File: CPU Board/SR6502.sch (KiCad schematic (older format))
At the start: 31 parts, among them J1 Conn_01x40_Female, SW1 RESET, SW2 SWA, SW3 SWA, SW4 SWA, SW5 SWA, SW6 SWA, U2 WD65C02_, U3 74HC00, U4 28C256, U5 CY62256-70PC, U6 WD65C22, U7 WC1602A, X1 1mhz

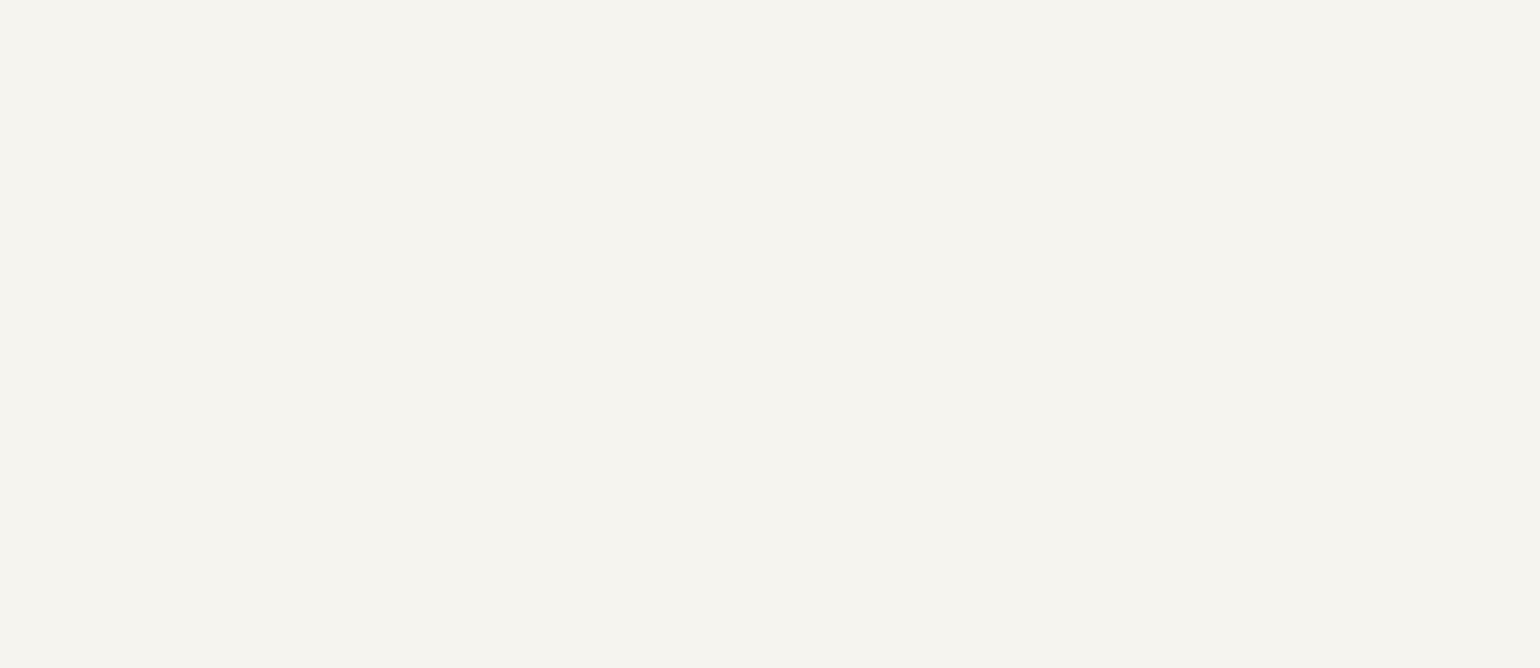
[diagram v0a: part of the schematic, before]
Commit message: Updated memory map, starting working on serial console
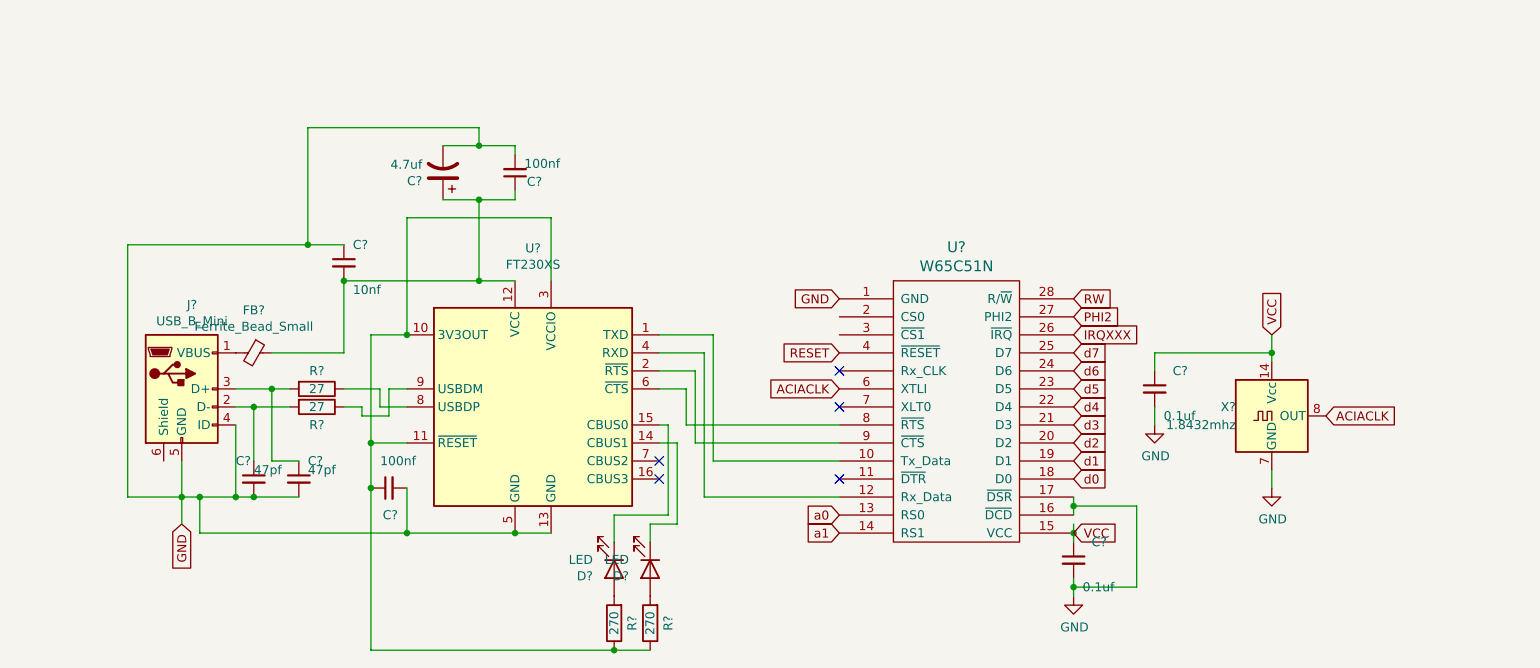
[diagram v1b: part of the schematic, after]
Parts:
- added C? (x2): 0.1uf, Capacitor_THT:C_Disc_D5.0mm_W2.5mm_P2.50mm, symbol Device:C_Small
- added C? (x2): 47pf, Capacitor_THT:C_Disc_D5.0mm_W2.5mm_P2.50mm, symbol Device:C_Small
- added C?: 10nf, Capacitor_THT:C_Disc_D5.0mm_W2.5mm_P2.50mm, symbol Device:C_Small
- added C? (x2): 100nf, Capacitor_THT:C_Disc_D5.0mm_W2.5mm_P2.50mm, symbol Device:C_Small
- added C?: 4.7uf, symbol Device:CP1
- added D? (x2): LED, symbol Device:LED
- added FB?: Ferrite_Bead_Small, symbol Device:Ferrite_Bead_Small
- added J?: USB_B_Mini, symbol Connector:USB_B_Mini
- added R? (x2): 270, Resistor_THT:R_Axial_DIN0204_L3.6mm_D1.6mm_P1.90mm_Vertical, symbol Device:R
- added R? (x2): 27, Resistor_THT:R_Axial_DIN0204_L3.6mm_D1.6mm_P1.90mm_Vertical, symbol Device:R
- added U?: W65C51N, symbol 65xx:W65C51N
- added U?: FT230XS, Package_SO:SSOP-16_3.9x4.9mm_P0.635mm, symbol Interface_USB:FT230XS
- added X?: 1.8432mhz, Package_DIP:DIP-14_W7.62mm_Socket, symbol Oscillator:ACO-xxxMHz
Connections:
- net GND: now also C?.1, C?.2, C?.2, C?.2, C?.2, C?.2, C?.2, C?.2, J?.4 (ID), J?.5 (GND), U?.1 (GND), U?.13 (GND), U?.16 (~DCD), U?.17 (~DSR), U?.5 (GND), X?.7 (GND)
- net PHI2: now also U?.27 (PHI2)
- net RESET: now also U?.4 (~RESET)
- net RW: now also U?.28 (R/~W)
- net VCC: now also C?.1, C?.1, U?.15 (VCC), X?.14 (Vcc)
- net a0: now also U?.13 (RS0)
- net a1: now also U?.14 (RS1)
- net d0: now also U?.18 (D0)
- net d1: now also U?.19 (D1)
- net d2: now also U?.20 (D2)
- net d3: now also U?.21 (D3)
- net d4: now also U?.22 (D4)
- net d5: now also U?.23 (D5)
- net d6: now also U?.24 (D6)
- net d7: now also U?.25 (D7)
- new net: U?.1 (TXD), U?.10 (Tx_Data)
- new net: U?.12 (Rx_Data), U?.4 (RXD)
- new net: U?.6 (~CTS), U?.8 (~RTS)
- new net: U?.2 (~RTS), U?.9 (~CTS)
- new net: C?.1, R?.1, R?.1, U?.10 (3V3OUT), U?.11 (~RESET), U?.3 (VCCIO)
- new net: C?.1, C?.1, C?.2, FB?.1, U?.12 (VCC)
- new net: D?.1 (K), U?.14 (CBUS1)
- new net: D?.1 (K), U?.15 (CBUS0)
- new net: R?.1, U?.8 (USBDP)
- new net: R?.1, U?.9 (USBDM)
- new net: D?.2 (A), R?.2 (x2)
- new net: FB?.2, J?.1 (VBUS)
- new net: C?.1, J?.2 (D-), R?.2
- new net: C?.1, J?.3 (D+), R?.2
- new net ACIACLK: U?.6 (XTLI), X?.8 (OUT)
- new net IRQXXX: U?.26 (~IRQ)
- no-connect marks 20 -> 25

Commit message: fixed errors in schematic (5 missing traces on pcb), did not export gerber yet
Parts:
- removed R3, R4, R5, R6, R7: 1k, Resistor_THT:R_Axial_DIN0204_L3.6mm_D1.6mm_P1.90mm_Vertical, symbol Device:R
- removed SW2, SW3, SW4, SW5, SW6: SWA, Button_Switch_THT:SW_Tactile_Straight_KSA0Axx1LFTR, symbol Switch:SW_Push
- added R? (x2): 3.3k, Resistor_THT:R_Axial_DIN0204_L3.6mm_D1.6mm_P1.90mm_Vertical, symbol Device:R
- J1: value Conn_01x40_Female -> Conn_02x40_Female; footprint Connector_PinSocket_2.54mm:PinSocket_1x40_P2.54mm_Vertical -> Connector_PinSocket_2.54mm:PinSocket_2x40_P2.54mm_Vertical; symbol Connector:Conn_01x40_Female -> Connector_Generic:Conn_02x40_Top_Bottom
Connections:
- net VCC: now also R?.1, R?.1; no longer U2.2 (RDY), U2.36 (BE), U3.1, U3.2
- net VIA1_CS2: now also U6.23 (~CS2)
- net a0: now also U6.38 (RS0)
- net a1: now also U6.37 (RS1)
- net a2: now also U6.36 (RS2)
- net a3: now also U6.35 (RS3)
- net DISPE: now reaches U6.9 (PA7), U7.6 (E)
- net VP: now reaches U2.1 (~VP)
- net VP: now also J1.34 (Pin_34)
- net PHI1O: now reaches U2.3 (PHI1out)
- net PHI1O: now also J1.36 (Pin_36)
- net SO: now reaches U2.38 (~SO)
- net SO: now also J1.35 (Pin_35)
- net PHI2O: now reaches U2.39 (PHI2out)
- net PHI2O: now also J1.37 (Pin_37)
- net ML: now reaches U2.5 (~ML)
- net ML: now also J1.33 (Pin_33)
- net SYNC: now reaches U2.7 (SYNC)
- net SYNC: now also J1.32 (Pin_32)
- net READY: now reaches J1.30 (Pin_30)
- net READY: now also U2.2 (RDY), R?.2
- net BE: now reaches J1.31 (Pin_31)
- net BE: now also U2.36 (BE), R?.2
- net ACIACLK: no longer names the net of U?.6 (XTLI), X?.8 (OUT)
- net B1: no longer names the net of U6.2 (PA0)
- net B2: no longer names the net of U6.3 (PA1)
- net B3: no longer names the net of U6.4 (PA2)
- net B4: no longer names the net of U6.5 (PA3)
- net B5: no longer names the net of U6.6 (PA4)
- no-connect marks 25 -> 22
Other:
- moved on the sheet: C?, U3A, X?

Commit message: changed memory map, added ACIA and 2nd VIA, irq matrix, added backplane pcb
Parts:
- removed C? (x2): 47pf, Capacitor_THT:C_Disc_D5.0mm_W2.5mm_P2.50mm, symbol Device:C_Small
- removed C?: 10nf, Capacitor_THT:C_Disc_D5.0mm_W2.5mm_P2.50mm, symbol Device:C_Small
- removed C? (x2): 100nf, Capacitor_THT:C_Disc_D5.0mm_W2.5mm_P2.50mm, symbol Device:C_Small
- removed C?: 4.7uf, symbol Device:CP1
- removed D? (x2): LED, symbol Device:LED
- removed FB?: Ferrite_Bead_Small, symbol Device:Ferrite_Bead_Small
- removed J?: USB_B_Mini, symbol Connector:USB_B_Mini
- removed R2: 1k, Resistor_THT:R_Axial_DIN0204_L3.6mm_D1.6mm_P1.90mm_Vertical, symbol Device:R
- removed R? (x2): 270, Resistor_THT:R_Axial_DIN0204_L3.6mm_D1.6mm_P1.90mm_Vertical, symbol Device:R
- removed R? (x2): 3.3k, Resistor_THT:R_Axial_DIN0204_L3.6mm_D1.6mm_P1.90mm_Vertical, symbol Device:R
- removed R? (x2): 27, Resistor_THT:R_Axial_DIN0204_L3.6mm_D1.6mm_P1.90mm_Vertical, symbol Device:R
- removed unit 4 of U3
- removed unit 3 of U3
- removed U?: FT230XS, Package_SO:SSOP-16_3.9x4.9mm_P0.635mm, symbol Interface_USB:FT230XS
- added C? (x5): 0.1uf, Capacitor_THT:C_Disc_D5.0mm_W2.5mm_P2.50mm, symbol Device:C
- added D? (x17): LED, symbol Device:LED
- added J?: Conn_02x12_Odd_Even_MountingPin, symbol Connector_Generic_MountingPin:Conn_02x12_Odd_Even_MountingPin
- added J? (x2): Conn_01x10_Female, symbol Connector:Conn_01x10_Female
- added J?: 5VDC INPUT, symbol Connector:Barrel_Jack
- added J?: ACIA1, symbol Connector:Conn_01x11_Female
- added R? (x17): 220, symbol Device:R_Small
- added RN?: 1k, Resistor_THT:R_Array_SIP6, symbol Device:R_Network05
- added RN? (x2): 3.3k, Resistor_THT:R_Array_SIP10, symbol Device:R_Network09
- added SW? (x5): SW_Push, symbol Switch:SW_Push
- added SW? (x2): SW_DIP_x08, symbol Switch:SW_DIP_x08
- added U? (x7): 74HC00, Package_DIP:DIP-14_W7.62mm_Socket, symbol 74xx:74HC00
- added U? (x2): 74LS30, symbol 74xx:74LS30
- added U? (x2): 74LS138, symbol 74xx:74LS138
- added U? (x3): 74HC21, symbol 74xx:74LS21
- R1: value 1k -> 3.3k
- RV1: footprint Potentiometer_THT:Potentiometer_Vishay_43_Horizontal -> Potentiometer_THT:Potentiometer_Vishay_T73XW_Horizontal
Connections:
- net IRQXXX is gone; now on net IRQ4: U?.26 (~IRQ)
- net BE: now also SW?.16
- net GND: now also J1.80 (Pin_80), C?.2, C?.2, C?.2, C?.2, C?.2, J?.2, J?.6 (Pin_6), R?.2, R?.2, R?.2, R?.2, R?.2, R?.2, R?.2, R?.2, R?.2, R?.2, SW?.1, SW?.1, SW?.1, SW?.1, SW?.1, U?.4 (E1), U?.7 (GND), U?.7 (GND), U?.7 (GND), U?.8 (GND), U?.8 (GND); no longer U4.22 (~OE), U?.16 (~DCD), U?.17 (~DSR)
- net IRQ: now also D?.1 (K), U?.8; no longer U6.21 (~IRQ)
- net NMI: now also SW?.9
- net PHI1O: no longer J1.36 (Pin_36)
- net PHI2: now also U?.5
- net PHI2O: no longer J1.37 (Pin_37)
- net READY: now also SW?.15
- net ROM_CS: now also D?.1 (K), J?.1 (Pin_1); no longer U3.5
- net RW: now also J?.18 (Pin_18), J?.24 (Pin_24), U?.1, U?.2; no longer U5.27 (~WE), U6.22 (R/~W), U?.28 (R/~W)
- net SRAM_CS: now also D?.1 (K), J?.7 (Pin_7)
- net VCC: now also J1.79 (Pin_79), C?.1, C?.1, C?.1, C?.1, C?.1, J?.1, J?.1 (Pin_1), J?.16 (Pin_16), J?.2 (Pin_2), J?.20 (Pin_20), J?.6 (Pin_6), R?.2, R?.2, R?.2, R?.2, R?.2, R?.2, R?.2, RN?.1 (common), RN?.1 (common), RN?.1 (common), U?.14 (VCC), U?.14 (VCC), U?.14 (VCC), U?.16 (VCC), U?.16 (VCC), U?.6 (E3); no longer U4.27 (~WE)
- net VIA1_CS2: now also D?.1 (K), J?.13 (Pin_13); no longer U3.6
- net a10: now also U?.4
- net a11: now also U?.5
- net a12: now also U?.6
- net a13: now also U?.11; no longer U6.24 (CS1)
- net a14: now also U?.12; no longer U3.4, U5.22 (~OE)
- net a15: now also U?.10, U?.9
- net a4: now also U?.1 (A0)
- net a5: now also U?.2 (A1)
- net a6: now also U?.3 (A2)
- net a7: now also U?.4 (E1), U?.6 (E3)
- net a8: now also U?.2
- net a9: now also U?.3
- net VIA1PB0: now reaches U6.10 (PB0), U7.7 (D0)
- net VIA1PB0: now also J?.1 (Pin_1)
- net VIA1PB1: now reaches U6.11 (PB1), U7.8 (D1)
- net VIA1PB1: now also J?.2 (Pin_2)
- net VIA1PB2: now reaches U6.12 (PB2), U7.9 (D2)
- net VIA1PB2: now also J?.3 (Pin_3)
- net VIA1PB3: now reaches U6.13 (PB3), U7.10 (D3)
- net VIA1PB3: now also J?.4 (Pin_4)
- net VIA1PB4: now reaches U6.14 (PB4), U7.11 (D4)
- net VIA1PB4: now also J?.5 (Pin_5)
- net VIA1PB5: now reaches U6.15 (PB5), U7.12 (D5)
- net VIA1PB5: now also J?.6 (Pin_6)
- net VIA1PB6: now reaches U6.16 (PB6), U7.13 (D6)
- net VIA1PB6: now also J?.7 (Pin_7)
- net VIA1PB7: now reaches U6.17 (PB7), U7.14 (D7)
- net VIA1PB7: now also J?.8 (Pin_8)
- net VIA1CB1: now reaches U6.18 (CB1)
- net VIA1CB1: now also J?.9 (Pin_9)
- net VIA1CB2: now reaches U6.19 (CB2)
- net VIA1CB2: now also J?.10 (Pin_10)
- net VIA1PA0: now reaches U6.2 (PA0)
- net VIA1PA0: now also J?.1 (Pin_1), RN?.2 (R1), SW?.2
- net VIA1PA1: now reaches U6.3 (PA1)
- net VIA1PA1: now also J?.2 (Pin_2), RN?.3 (R2), SW?.2
- net VIA1CA2: now reaches U6.39 (CA2)
- net VIA1CA2: now also J?.10 (Pin_10)
- net VIA1PA2: now reaches U6.4 (PA2)
- net VIA1PA2: now also J?.3 (Pin_3), RN?.4 (R3), SW?.2
- net VIA1CA1: now reaches U6.40 (CA1)
- net VIA1CA1: now also J?.9 (Pin_9)
- net VIA1PA3: now reaches U6.5 (PA3)
- net VIA1PA3: now also J?.4 (Pin_4), RN?.5 (R4), SW?.2
- net VIA1PA4: now reaches U6.6 (PA4)
- net VIA1PA4: now also J?.5 (Pin_5), RN?.6 (R5), SW?.2
- net VIA1PA5: now reaches U6.7 (PA5), U7.4 (RS)
- net VIA1PA5: now also J?.6 (Pin_6)
- net VIA1PA6: now reaches U6.8 (PA6), U7.5 (R/W)
- net VIA1PA6: now also J?.7 (Pin_7)
- net IRQ1: now reaches J1.41 (Pin_41)
- net IRQ1: now also D?.1 (K), SW?.16, U?.1
- net IRQ2: now reaches J1.42 (Pin_42)
- net IRQ2: now also D?.1 (K), SW?.15, U?.2
- net IRQ3: now reaches J1.43 (Pin_43)
- net IRQ3: now also D?.1 (K), SW?.14, U?.4
- net IRQ4: now reaches J1.44 (Pin_44)
- net IRQ4: now also D?.1 (K), SW?.13, U?.5
- net IRQ5: now reaches J1.45 (Pin_45)
- net IRQ5: now also D?.1 (K), SW?.12, U?.9
- net IRQ6: now reaches J1.46 (Pin_46)
- net IRQ6: now also D?.1 (K), SW?.11, U?.10
- net IRQ7: now reaches J1.47 (Pin_47)
- net IRQ7: now also U6.21 (~IRQ), D?.1 (K), SW?.10, U?.12
- net $60XX: now reaches J1.48 (Pin_48)
- net $61XX: now reaches J1.49 (Pin_49)
- net $62XX: now reaches J1.50 (Pin_50)
- net $63XX: now reaches J1.51 (Pin_51)
- net $64XX: now reaches J1.52 (Pin_52)
- net $65XX: now reaches J1.53 (Pin_53)
- net $66XX: now reaches J1.54 (Pin_54)
- net $67XX: now reaches J1.55 (Pin_55)
- net ACIA_CLOCK: now reaches J1.78 (Pin_78)
- net ACIA_CLOCK: now also U?.6 (XTLI), X?.8 (OUT)
- net ACIA1_TXD: now reaches U?.10 (Tx_Data)
- net ACIA1_TXD: now also J?.5 (Pin_5)
- net ACIA1_DTR: now reaches U?.11 (~DTR)
- net ACIA1_DTR: now also J?.9 (Pin_9)
- net ACIA1_RXD: now reaches U?.12 (Rx_Data)
- net ACIA1_RXD: now also J?.4 (Pin_4)
- net ACIA1_CS0: now reaches U?.2 (CS0)
- net ACIA1_CS0: now also D?.2 (A), J?.19 (Pin_19)
- net ACIA2_CS1: now reaches U?.3 (~CS1)
- net ACIA2_CS1: now also D?.1 (K), J?.21 (Pin_21)
- net ACIA1_RTS: now reaches U?.8 (~RTS)
- net ACIA1_RTS: now also J?.11 (Pin_11)
- net ACIA1_CTS: now reaches U?.9 (~CTS)
- net ACIA1_CTS: now also J?.10 (Pin_10)
- net DISPE renamed VIA1PA7
- net VIA1PA7: now also J?.8 (Pin_8)
- new net: D?.2 (A), R?.1 (x15)
- new net: D?.1 (K), R?.1 (x2)
- new net: U?.13, U?.6
- new net: RN?.2 (R1), SW?.1 (x2)
- new net: RN?.3 (R2), SW?.2 (x2)
- new net: RN?.4 (R3), SW?.3 (x2)
- new net: RN?.5 (R4), SW?.4 (x2)
- new net: RN?.6 (R5), SW?.5 (x2)
- new net: RN?.7 (R6), SW?.6 (x2)
- new net: RN?.8 (R7), SW?.7 (x2)
- new net: RN?.9 (R8), SW?.8 (x2)
- new net $7F0X: J?.14 (Pin_14), U?.15 (O0)
- new net $7F1X: J?.22 (Pin_22), U?.14 (O1)
- new net $7F2X: U?.13 (O2)
- new net $7F3X: U?.12 (O3)
- new net $7F4X: U?.11 (O4)
- new net $7F5X: U?.10 (O5)
- new net $7F6X: U?.9 (O6)
- new net $7F7X: U?.7 (O7)
- new net $7F8X: U?.15 (O0)
- new net $7F9X: U?.14 (O1)
- new net $7FAX: U?.13 (O2)
- new net $7FBX: U?.12 (O3)
- new net $7FCX: U?.11 (O4)
- new net $7FDX: U?.10 (O5)
- new net $7FEX: U?.9 (O6)
- new net $7FFX: U?.7 (O7)
- new net $7FXX: U?.13, U?.5 (E2), U?.5 (E2), U?.8
- new net ACIA1_DCD: J?.8 (Pin_8), U?.16 (~DCD)
- new net ACIA1_DSR: J?.7 (Pin_7), U?.17 (~DSR)
- new net ACIA1_RW: J?.23 (Pin_23), U?.28 (R/~W)
- new net MRD: J?.10 (Pin_10), J?.4 (Pin_4), U?.3, U?.4
- new net MWR: J?.12 (Pin_12), U?.6
- new net RAMSEL: J?.8 (Pin_8), U?.11
- new net ROMSEL: J?.2 (Pin_2), U?.1, U?.12, U?.8
- new net ROM_OE: D?.1 (K), J?.3 (Pin_3), U4.22 (~OE)
- new net ROM_WE: J?.5 (Pin_5), U4.27 (~WE)
- new net SRAM_OE: D?.1 (K), J?.9 (Pin_9), U5.22 (~OE)
- new net SRAM_WE: D?.1 (K), J?.11 (Pin_11), U5.27 (~WE)
- new net VIA_CS1: D?.2 (A), J?.15 (Pin_15), U6.24 (CS1)
- new net VIA_RW: J?.17 (Pin_17), U6.22 (R/~W)
- no-connect marks 22 -> 10
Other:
- note added: "$8000-FFFF"
- note added: "0000-3FFF"
- note added: "7F00-7FFF\n"
- moved on the sheet: C5, C?, U3A, U3E, U?, X?

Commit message: Final push to JLCPCB for latest rev
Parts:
- removed C5: 0.1uf, Capacitor_THT:C_Disc_D5.0mm_W2.5mm_P2.50mm, symbol Device:C
- removed C7: 0.1uf, Capacitor_THT:C_Disc_D5.0mm_W2.5mm_P2.50mm, symbol Device:C_Small
- removed D? (x17): LED, symbol Device:LED
- removed JP1: Jumper, Connector_PinSocket_2.54mm:PinSocket_1x02_P2.54mm_Vertical, symbol Device:Jumper
- removed R1: 3.3k, Resistor_THT:R_Axial_DIN0204_L3.6mm_D1.6mm_P1.90mm_Vertical, symbol Device:R_Small
- removed R? (x17): 220, symbol Device:R_Small
- removed RN?: 1k, Resistor_THT:R_Array_SIP6, symbol Device:R_Network05
- removed U3, U? (x2): 74HC00, Package_DIP:DIP-14_W7.62mm_Socket, symbol 74xx:74HC00
- added C12, C2: CP, Capacitor_THT:CP_Radial_Tantal_D4.5mm_P2.50mm, symbol Device:CP
- added C16, C17, C18, C19, C20, C21, C22, C23: 0.1uf, Capacitor_THT:C_Disc_D5.0mm_W2.5mm_P2.50mm, symbol Device:C
- added SW9: SW_Push, Button_Switch_THT:SW_Tactile_Straight_KSA0Axx1LFTR, symbol Switch:SW_Push
- added U13: DS1813-5, Package_TO_SOT_THT:TO-92_Inline, symbol DS1813-5:DS1813-5
- J1: renamed from J?; footprint (none) -> Connector_BarrelJack:BarrelJack_Horizontal
- J2: renamed from J?; value Conn_02x12_Odd_Even_MountingPin -> Conn_02x16_Odd_Even_MountingPin; footprint (none) -> Connector_PinHeader_2.54mm:PinHeader_2x12_P2.54mm_Vertical; symbol Connector_Generic_MountingPin:Conn_02x12_Odd_Even_MountingPin -> Connector_Generic:Conn_02x12_Odd_Even
- J3, J4: renamed from J?; footprint (none) -> Connector_PinSocket_2.54mm:PinSocket_1x10_P2.54mm_Vertical
- J5: renamed from J?; footprint (none) -> Connector_PinSocket_2.54mm:PinSocket_1x11_P2.54mm_Vertical
- J6: renamed from J1; footprint Connector_PinSocket_2.54mm:PinSocket_2x40_P2.54mm_Vertical -> Connector_PinHeader_2.54mm:PinHeader_2x40_P2.54mm_Horizontal; symbol Connector_Generic:Conn_02x40_Top_Bottom -> Connector_Generic:Conn_02x40_Odd_Even
- SW2, SW3: renamed from SW?; footprint (none) -> Button_Switch_THT:SW_DIP_SPSTx08_Slide_9.78x22.5mm_W7.62mm_P2.54mm
- SW4, SW5, SW6, SW7, SW8: renamed from SW?; footprint (none) -> Button_Switch_THT:SW_Tactile_Straight_KSA0Axx1LFTR
- U11: renamed from U?; footprint (none) -> Package_DIP:DIP-28_W15.24mm
- U3, U6: renamed from U?; footprint (none) -> Package_DIP:DIP-14_W7.62mm_Socket
- U7, U8: renamed from U?; footprint (none) -> Package_DIP:DIP-16_W7.62mm_Socket
- X1: footprint Package_DIP:DIP-14_W7.62mm_Socket -> Oscillator:Oscillator_DIP-14
- X2: renamed from X?; footprint Package_DIP:DIP-14_W7.62mm_Socket -> Oscillator:Oscillator_DIP-14
- gave numbers to parts that had none: 10
- renumbered C8 to C3, C2 to C4, C3 to C5, C4 to C6, C6 to C9, U2 to U1, U7 to U10, U6 to U9
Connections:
- net $61XX is gone; now on net PHI2: J6.49 (Pin_49)
- net $63XX is gone; now on net RESET: J6.51 (Pin_51)
- net $65XX is gone; now on net RW: J6.53 (Pin_53)
- net $67XX is gone; now on net IRQ: J6.55 (Pin_55)
- net $7F0X: now also J6.16 (Pin_16), U7.15 (O0); no longer U8.15 (O0)
- net $7F1X: now also J6.18 (Pin_18), U7.14 (O1); no longer U8.14 (O1)
- net $7F2X: now also J6.20 (Pin_20), U7.13 (O2); no longer U8.13 (O2)
- net $7F3X: now also J6.22 (Pin_22), U7.12 (O3); no longer U8.12 (O3)
- net $7F4X: now also J6.24 (Pin_24), U7.11 (O4); no longer U8.11 (O4)
- net $7F5X: now also J6.26 (Pin_26), U7.10 (O5); no longer U8.10 (O5)
- net $7F6X: now also J6.28 (Pin_28), U7.9 (O6); no longer U8.9 (O6)
- net $7F7X: now also J6.30 (Pin_30), U7.7 (O7); no longer U8.7 (O7)
- net $7F8X: now also J6.32 (Pin_32), U8.15 (O0); no longer U7.15 (O0)
- net $7F9X: now also J6.34 (Pin_34), U8.14 (O1); no longer U7.14 (O1)
- net $7FAX: now also J6.36 (Pin_36), U8.13 (O2); no longer U7.13 (O2)
- net $7FBX: now also J6.38 (Pin_38), U8.12 (O3); no longer U7.12 (O3)
- net $7FCX: now also J6.40 (Pin_40), U8.11 (O4); no longer U7.11 (O4)
- net $7FDX: now also J6.42 (Pin_42), U8.10 (O5); no longer U7.10 (O5)
- net $7FEX: now also J6.44 (Pin_44), U8.9 (O6); no longer U7.9 (O6)
- net $7FFX: now also J6.46 (Pin_46), U8.7 (O7); no longer U7.7 (O7)
- net ACIA_CLOCK: no longer J6.78 (Pin_78)
- net BE: now also J6.61 (Pin_61); no longer J6.31 (Pin_31)
- net GND: now also J6.79 (Pin_79), U8.4 (E1), C12.2, C16.2, C17.2, C18.2, C19.2, C2.2, C20.2, C21.2, C22.2, C23.2, SW9.2, U13.3 (GND); no longer J6.40 (Pin_40), U7.4 (E1)
- net IRQ: no longer J6.28 (Pin_28)
- net IRQ1: now also J6.2 (Pin_2), SW2.10, U6.12; no longer J6.41 (Pin_41), SW2.16, U6.1
- net IRQ2: now also J6.4 (Pin_4), SW2.11, U6.10; no longer J6.42 (Pin_42), SW2.15, U6.2
- net IRQ3: now also J6.6 (Pin_6), SW2.12, U6.9; no longer J6.43 (Pin_43), SW2.14, U6.4
- net IRQ4: now also J6.8 (Pin_8); no longer J6.44 (Pin_44)
- net IRQ5: now also J6.10 (Pin_10), SW2.14, U6.4; no longer J6.45 (Pin_45), SW2.12, U6.9
- net IRQ6: now also J6.12 (Pin_12), SW2.15, U6.2; no longer J6.46 (Pin_46), SW2.11, U6.10
- net IRQ7: now also J6.14 (Pin_14), SW2.16, U6.1; no longer J6.47 (Pin_47), SW2.10, U6.12
- net ML: now also J6.65 (Pin_65); no longer J6.33 (Pin_33)
- net NMI: now also J6.57 (Pin_57), SW9.1; no longer J6.29 (Pin_29)
- net PHI2: now also X1.8 (OUT); no longer J6.25 (Pin_25)
- net READY: now also J6.59 (Pin_59); no longer J6.30 (Pin_30)
- net RESET: now also SW3.14, U13.1 (*RST); no longer J6.26 (Pin_26)
- net RW: no longer J6.27 (Pin_27)
- net SO: now also J6.69 (Pin_69); no longer J6.35 (Pin_35)
- net SYNC: now also J6.63 (Pin_63); no longer J6.32 (Pin_32)
- net VCC: now also J6.77 (Pin_77), J6.78 (Pin_78), U7.6 (E3), C12.1, C16.1, C17.1, C18.1, C19.1, C2.1, C20.1, C21.1, C22.1, C23.1, U13.2 (VCC); no longer J6.39 (Pin_39), J6.79 (Pin_79), U8.6 (E3)
- net VIA1PA0: now also SW3.9
- net VIA1PA1: now also SW3.10
- net VIA1PA2: now also SW3.11
- net VIA1PA3: now also SW3.12
- net VIA1PA4: now also SW3.13
- net VP: now also J6.67 (Pin_67); no longer J6.34 (Pin_34)
- net a1: now also J6.3 (Pin_3); no longer J6.2 (Pin_2)
- net a10: now also J6.21 (Pin_21); no longer J6.11 (Pin_11)
- net a11: now also J6.23 (Pin_23); no longer J6.12 (Pin_12)
- net a12: now also J6.25 (Pin_25); no longer J6.13 (Pin_13)
- net a13: now also J6.27 (Pin_27); no longer J6.14 (Pin_14)
- net a14: now also J6.29 (Pin_29); no longer J6.15 (Pin_15)
- net a15: now also J6.31 (Pin_31); no longer J6.16 (Pin_16)
- net a2: now also J6.5 (Pin_5); no longer J6.3 (Pin_3)
- net a3: now also J6.7 (Pin_7); no longer J6.4 (Pin_4)
- net a4: now also J6.9 (Pin_9), U7.1 (A0); no longer J6.5 (Pin_5)
- net a5: now also J6.11 (Pin_11), U7.2 (A1); no longer J6.6 (Pin_6)
- net a6: now also J6.13 (Pin_13), U7.3 (A2); no longer J6.7 (Pin_7)
- net a7: now also J6.15 (Pin_15), U7.4 (E1), U8.6 (E3); no longer J6.8 (Pin_8), U7.6 (E3), U8.4 (E1)
- net a8: now also J6.17 (Pin_17); no longer J6.9 (Pin_9)
- net a9: now also J6.19 (Pin_19); no longer J6.10 (Pin_10)
- net d0: now also J6.33 (Pin_33); no longer J6.17 (Pin_17)
- net d1: now also J6.35 (Pin_35); no longer J6.18 (Pin_18)
- net d2: now also J6.37 (Pin_37); no longer J6.19 (Pin_19)
- net d3: now also J6.39 (Pin_39); no longer J6.20 (Pin_20)
- net d4: now also J6.41 (Pin_41); no longer J6.21 (Pin_21)
- net d5: now also J6.43 (Pin_43); no longer J6.22 (Pin_22)
- net d6: now also J6.45 (Pin_45); no longer J6.23 (Pin_23)
- net d7: now also J6.47 (Pin_47); no longer J6.24 (Pin_24)
- net $60XX: no longer names the net of J6.48 (Pin_48)
- net $62XX: no longer names the net of J6.50 (Pin_50)
- net $64XX: no longer names the net of J6.52 (Pin_52)
- net $66XX: no longer names the net of J6.54 (Pin_54)
- net ACIA2_CS1 renamed ACIA1_CS1
- net PHI1O: no longer names the net of U1.3 (PHI1out)
- net PHI2O: no longer names the net of U1.39 (PHI2out)
- no-connect marks 10 -> 36
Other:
- note removed: "$8000-FFFF"
- note removed: "0000-3FFF"
- moved on the sheet: RN2, SW1, SW3
